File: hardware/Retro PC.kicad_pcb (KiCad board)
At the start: 2 copper layers, 160 x 160 mm, 70 parts, among them IC1 74HC00, IC10 W65C22, IC11 LCD-016N002L, IC2 W65C02, IC3 74HC138, IC4 SYSTEM ROM, IC5 AS6C62256A, IC6 W65C22, IC7 W65C51, IC8 TL7702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

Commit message: Working on layout
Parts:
- removed C19: 100nF, Capacitor_THT:C_Rect_L4.0mm_W2.5mm_P2.50mm
- removed J1: USB_B, TE_Connectivity:USB_B_TE_2923042_Horizontal
- added X2: USB_B, Connector_Custom:USB-B_TE_2923042_Horizontal, F.Cu at (220.2, 158.6)
- added X4: KEYBOARD, Connector_Custom:Mini-DIN_TE_Female_6Pin_2rows, F.Cu at (230.1, 178.0)
- X1: value ConBarrel -> DC IN; footprint Wuerth:BarrelJack_Wuerth_6941xx301002 -> Connector_Custom:BarrelJack_Wuerth_6941xx301002
- X3: renamed from J3; value Conn_02x20_Odd_Even -> Expansion
- moved C18 112.0 mm to (147.8, 187.6), turned to 90 degrees
- moved D9 67.1 mm to (204.4, 117.1), turned to 180 degrees
- moved R1 8.01 mm to (159.3, 81.3), turned to 90 degrees
- moved D8 7.24 mm to (163.7, 73.7), turned to 270 degrees
- moved D13 6.10 mm to (71.4, 73.5)
- moved R8 6.10 mm to (78.5, 69.3)
- moved X3 1.02 mm to (220.1, 72.6)
- moved IC5 0.07 mm to (109.9, 119.6)
- moved IC4 0.06 mm to (109.9, 87.8)
- moved C4 0.06 mm to (109.9, 108.9), turned to 0 degrees
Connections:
- net /IO/1MHz renamed /IO/Clock
- net /Processor/ModemReady renamed /Processor/~ModemReady
- D9 pad 1: /Processor/~IRQ -> /IO/~IRQ
- IC10 pad 10: Net-(IC10-Pad10) -> /LCD / PS2/LCD0
- IC10 pad 11: Net-(IC10-Pad11) -> /LCD / PS2/LCD1
- IC10 pad 12: Net-(IC10-Pad12) -> /LCD / PS2/LCD2
- IC10 pad 13: Net-(IC10-Pad13) -> (no net)
- IC10 pad 14: Net-(IC10-Pad14) -> (no net)
- IC10 pad 15: Net-(IC10-Pad15) -> (no net)
- IC10 pad 16: Net-(IC10-Pad16) -> /LCD / PS2/PS20
- IC10 pad 17: Net-(IC10-Pad17) -> /LCD / PS2/PS21
- IC10 pad 18: Net-(IC10-Pad18) -> (no net)
- IC10 pad 19: Net-(IC10-Pad19) -> (no net)
- IC10 pad 2: Net-(IC10-Pad2) -> /LCD / PS2/LCD3
- IC10 pad 3: Net-(IC10-Pad3) -> /LCD / PS2/LCD4
- IC10 pad 39: Net-(IC10-Pad39) -> (no net)
- IC10 pad 4: Net-(IC10-Pad4) -> /LCD / PS2/LCD5
- IC10 pad 40: Net-(IC10-Pad40) -> (no net)
- IC10 pad 5: Net-(IC10-Pad5) -> /LCD / PS2/LCD6
- IC10 pad 6: Net-(IC10-Pad6) -> /LCD / PS2/LCD7
- IC10 pad 7: Net-(IC10-Pad7) -> /LCD / PS2/LCD8
- IC10 pad 8: Net-(IC10-Pad8) -> /LCD / PS2/LCD9
- IC10 pad 9: Net-(IC10-Pad9) -> /LCD / PS2/LCD10
- IC11 pad 10: Net-(IC11-Pad10) -> /LCD / PS2/LCD6
- IC11 pad 11: Net-(IC11-Pad11) -> /LCD / PS2/LCD7
- IC11 pad 12: Net-(IC11-Pad12) -> /LCD / PS2/LCD8
- IC11 pad 13: Net-(IC11-Pad13) -> /LCD / PS2/LCD9
- IC11 pad 14: Net-(IC11-Pad14) -> /LCD / PS2/LCD10
- IC11 pad 4: Net-(IC11-Pad4) -> /LCD / PS2/LCD2
- IC11 pad 5: Net-(IC11-Pad5) -> /LCD / PS2/LCD1
- IC11 pad 6: Net-(IC11-Pad6) -> /LCD / PS2/LCD0
- IC11 pad 7: Net-(IC11-Pad7) -> /LCD / PS2/LCD3
- IC11 pad 8: Net-(IC11-Pad8) -> /LCD / PS2/LCD4
- IC11 pad 9: Net-(IC11-Pad9) -> /LCD / PS2/LCD5
- IC11 pad A1: Net-(IC11-PadA1) -> (no net)
- IC11 pad A2: Net-(IC11-PadA2) -> (no net)
- IC11 pad K1: Net-(IC11-PadK1) -> (no net)
- IC11 pad K2: Net-(IC11-PadK2) -> (no net)
- IC2 pad 1: /Processor/VPB -> (no net)
- IC2 pad 3: Net-(IC2-Pad3) -> (no net)
- IC2 pad 35: Net-(IC2-Pad35) -> (no net)
- IC2 pad 36: /Processor/BE -> (no net)
- IC2 pad 38: Net-(IC2-Pad38) -> (no net)
- IC2 pad 39: Net-(IC2-Pad39) -> (no net)
- IC2 pad 5: Net-(IC2-Pad5) -> (no net)
- IC2 pad 7: /Processor/SYNC -> (no net)
- IC3 pad 10: Net-(IC3-Pad10) -> (no net)
- IC3 pad 11: Net-(IC3-Pad11) -> (no net)
- IC3 pad 12: Net-(IC3-Pad12) -> (no net)
- IC3 pad 7: Net-(IC3-Pad7) -> (no net)
- IC3 pad 9: Net-(IC3-Pad9) -> (no net)
- IC6 pad 39: Net-(IC6-Pad39) -> (no net)
- IC6 pad 40: Net-(IC6-Pad40) -> (no net)
- IC7 pad 11: /Processor/ACIAReady -> (no net)
- IC7 pad 16: GND -> (no net)
- IC7 pad 5: Net-(IC7-Pad5) -> (no net)
- IC8 pad 6: Net-(IC8-Pad6) -> (no net)
- IC9 pad 10: Net-(IC9-Pad10) -> (no net)
- IC9 pad 12: Net-(IC9-Pad12) -> (no net)
- IC9 pad 13: Net-(IC9-Pad13) -> (no net)
- IC9 pad 14: Net-(IC9-Pad14) -> (no net)
- IC9 pad 26: Net-(IC9-Pad26) -> (no net)
- IC9 pad 27: Net-(IC9-Pad27) -> (no net)
- IC9 pad 28: Net-(IC9-Pad28) -> (no net)
- IC9 pad 6: Net-(IC9-Pad6) -> (no net)
- IC9 pad 9: Net-(IC9-Pad9) -> (no net)
- RV1 pad 3: Net-(RV1-Pad3) -> (no net)
- X3 pad 24: Net-(J3-Pad24) -> /IO/~IRQ
- X3 pad 26: Net-(J3-Pad26) -> (no net)
- X3 pad 28: Net-(J3-Pad28) -> (no net)
- X3 pad 30: Net-(J3-Pad30) -> (no net)
- X3 pad 32: Net-(J3-Pad32) -> (no net)
- X3 pad 33: Net-(J3-Pad33) -> (no net)
- X3 pad 34: Net-(J3-Pad34) -> (no net)
- X3 pad 35: Net-(J3-Pad35) -> (no net)
- X3 pad 36: Net-(J3-Pad36) -> (no net)
- X3 pad 37: Net-(J3-Pad37) -> (no net)
- X3 pad 38: Net-(J3-Pad38) -> (no net)
- XTAL1 pad 1: Net-(XTAL1-Pad1) -> (no net)
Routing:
- net /LCD / PS2/PS20: track 0.00 -> 98.2 mm, vias 0 -> 1
- net /LCD / PS2/PS21: track 0.00 -> 93.1 mm, vias 0 -> 1
- net /IO/D7: track 323.3 -> 402.6 mm, vias 12 -> 13
- net /IO/D6: track 327.3 -> 401.7 mm, vias 13 -> 14
- net /IO/D5: track 330.7 -> 398.2 mm, vias 13 -> 14
- net /IO/D4: track 334.5 -> 395.3 mm, vias 13 -> 14
- net /IO/D3: track 335.2 -> 391.5 mm, vias 13 -> 14
- net /IO/R~W: track 180.3 -> 232.3 mm, vias 9 -> 11
- net /IO/D2: track 352.7 -> 401.7 mm, vias 11 -> 12
- net /IO/Clock: track 153.2 -> 202.1 mm, vias 5 -> 8
- net /IO/D1: track 361.5 -> 404.8 mm, vias 11 -> 12
- net /Processor/~IRQ_ACIA: track 37.4 -> 76.8 mm
- net /IO/~RESET: track 365.0 -> 404.3 mm, vias 8 -> 10
- net /IO/D0: track 370.0 -> 404.0 mm, vias 11 -> 12
- net /IO/~IRQ: track 0.00 -> 33.6 mm, vias 0 -> 1
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
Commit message: First version of the layout
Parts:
- U1: value R-785.0-0.5 -> R-785.0-1.0
- X2: value USB_B -> SERIAL
- moved D14 4.42 mm to (146.4, 169.0), turned to 180 degrees
- moved XTAL2 0.66 mm to (189.2, 146.2)
- moved R4 0.53 mm to (195.5, 141.0)
- moved C8 0.51 mm to (183.8, 146.2)
- moved C11 0.38 mm to (117.1, 55.2)
- moved C17 0.33 mm to (130.8, 55.2)
- moved R9 0.18 mm to (123.2, 52.0)
- moved R5 0.14 mm to (109.5, 52.0)
- moved SW1 0.12 mm to (110.6, 44.0)
- moved SW4 0.06 mm to (124.3, 44.0)
- turned C18 to 270 degrees
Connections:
- IC10 pad 13: (no net) -> Net-(IC10-Pad13)
- IC10 pad 14: (no net) -> Net-(IC10-Pad14)
- IC10 pad 15: (no net) -> Net-(IC10-Pad15)
- IC10 pad 18: (no net) -> Net-(IC10-Pad18)
- IC10 pad 19: (no net) -> Net-(IC10-Pad19)
- IC10 pad 39: (no net) -> Net-(IC10-Pad39)
- IC10 pad 40: (no net) -> Net-(IC10-Pad40)
- IC11 pad A1: (no net) -> Net-(IC11-PadA1)
- IC11 pad A2: (no net) -> Net-(IC11-PadA2)
- IC11 pad K1: (no net) -> Net-(IC11-PadK1)
- IC11 pad K2: (no net) -> Net-(IC11-PadK2)
- IC2 pad 1: (no net) -> /Processor/VPB
- IC2 pad 3: (no net) -> Net-(IC2-Pad3)
- IC2 pad 35: (no net) -> Net-(IC2-Pad35)
- IC2 pad 36: (no net) -> /Processor/BE
- IC2 pad 38: (no net) -> Net-(IC2-Pad38)
- IC2 pad 39: (no net) -> Net-(IC2-Pad39)
- IC2 pad 5: (no net) -> Net-(IC2-Pad5)
- IC2 pad 7: (no net) -> /Processor/SYNC
- IC3 pad 10: (no net) -> Net-(IC3-Pad10)
- IC3 pad 11: (no net) -> Net-(IC3-Pad11)
- IC3 pad 12: (no net) -> Net-(IC3-Pad12)
- IC3 pad 7: (no net) -> Net-(IC3-Pad7)
- IC3 pad 9: (no net) -> Net-(IC3-Pad9)
- IC6 pad 39: (no net) -> Net-(IC6-Pad39)
- IC6 pad 40: (no net) -> Net-(IC6-Pad40)
- IC7 pad 11: (no net) -> /Processor/~ReceiverReady
- IC7 pad 16: (no net) -> /Processor/~Carrier
- IC7 pad 5: (no net) -> Net-(IC7-Pad5)
- IC8 pad 6: (no net) -> Net-(IC8-Pad6)
- IC9 pad 10: (no net) -> Net-(IC9-Pad10)
- IC9 pad 12: (no net) -> Net-(IC9-Pad12)
- IC9 pad 13: (no net) -> Net-(IC9-Pad13)
- IC9 pad 14: (no net) -> Net-(IC9-Pad14)
- IC9 pad 26: (no net) -> Net-(IC9-Pad26)
- IC9 pad 27: (no net) -> Net-(IC9-Pad27)
- IC9 pad 28: (no net) -> Net-(IC9-Pad28)
- IC9 pad 6: (no net) -> Net-(IC9-Pad6)
- IC9 pad 9: (no net) -> Net-(IC9-Pad9)
- RV1 pad 3: (no net) -> Net-(RV1-Pad3)
- X2 pad 1: (no net) -> Net-(X2-Pad1)
- X3 pad 26: (no net) -> Net-(X3-Pad26)
- X3 pad 28: (no net) -> Net-(X3-Pad28)
- X3 pad 30: (no net) -> Net-(X3-Pad30)
- X3 pad 32: (no net) -> Net-(X3-Pad32)
- X3 pad 33: (no net) -> Net-(X3-Pad33)
- X3 pad 34: (no net) -> Net-(X3-Pad34)
- X3 pad 35: (no net) -> Net-(X3-Pad35)
- X3 pad 36: (no net) -> Net-(X3-Pad36)
- X3 pad 37: (no net) -> Net-(X3-Pad37)
- X3 pad 38: (no net) -> Net-(X3-Pad38)
- X4 pad 3: (no net) -> Net-(X4-Pad3)
- X4 pad 6: (no net) -> Net-(X4-Pad6)
- X4 pad 7: (no net) -> GND
- XTAL1 pad 1: (no net) -> Net-(XTAL1-Pad1)
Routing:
- net /LCD / PS2/LCD10: track 0.00 -> 93.8 mm, vias 0 -> 1
- net /LCD / PS2/LCD9: track 0.00 -> 93.4 mm, vias 0 -> 1
- net /LCD / PS2/LCD8: track 0.00 -> 92.9 mm, vias 0 -> 1
- net /LCD / PS2/LCD7: track 0.00 -> 92.5 mm, vias 0 -> 1
- net /LCD / PS2/LCD6: track 0.00 -> 92.0 mm, vias 0 -> 1
- net /LCD / PS2/LCD5: track 0.00 -> 91.6 mm, vias 0 -> 1
- net /LCD / PS2/LCD4: track 0.00 -> 91.4 mm, vias 0 -> 1
- net /LCD / PS2/LCD3: track 0.00 -> 90.9 mm, vias 0 -> 1
- net /Processor/~IRQ_ACIA: track 76.8 -> 166.9 mm, vias 2 -> 6
- net /LCD / PS2/LCD0: track 0.00 -> 83.1 mm, vias 0 -> 3
- net Net-(IC11-Pad3): track 0.00 -> 81.9 mm, vias 0 -> 2
- net /LCD / PS2/LCD1: track 0.00 -> 79.2 mm, vias 0 -> 3
- net /LCD / PS2/LCD2: track 0.00 -> 75.6 mm, vias 0 -> 3
- net /Processor/~CS_VIA_2: track 76.8 -> 75.7 mm
- net Net-(C8-Pad1): track 17.4 -> 18.5 mm
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
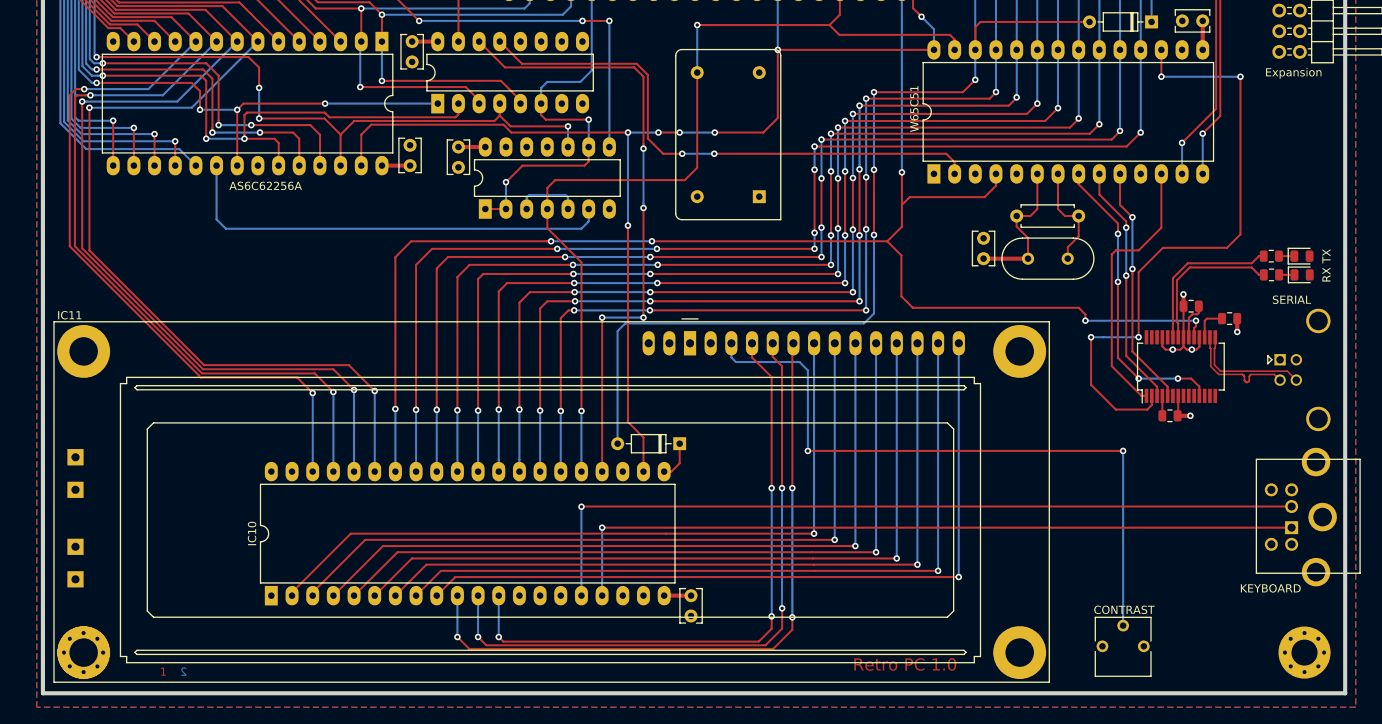
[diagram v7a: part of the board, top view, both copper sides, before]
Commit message: Replace LCD
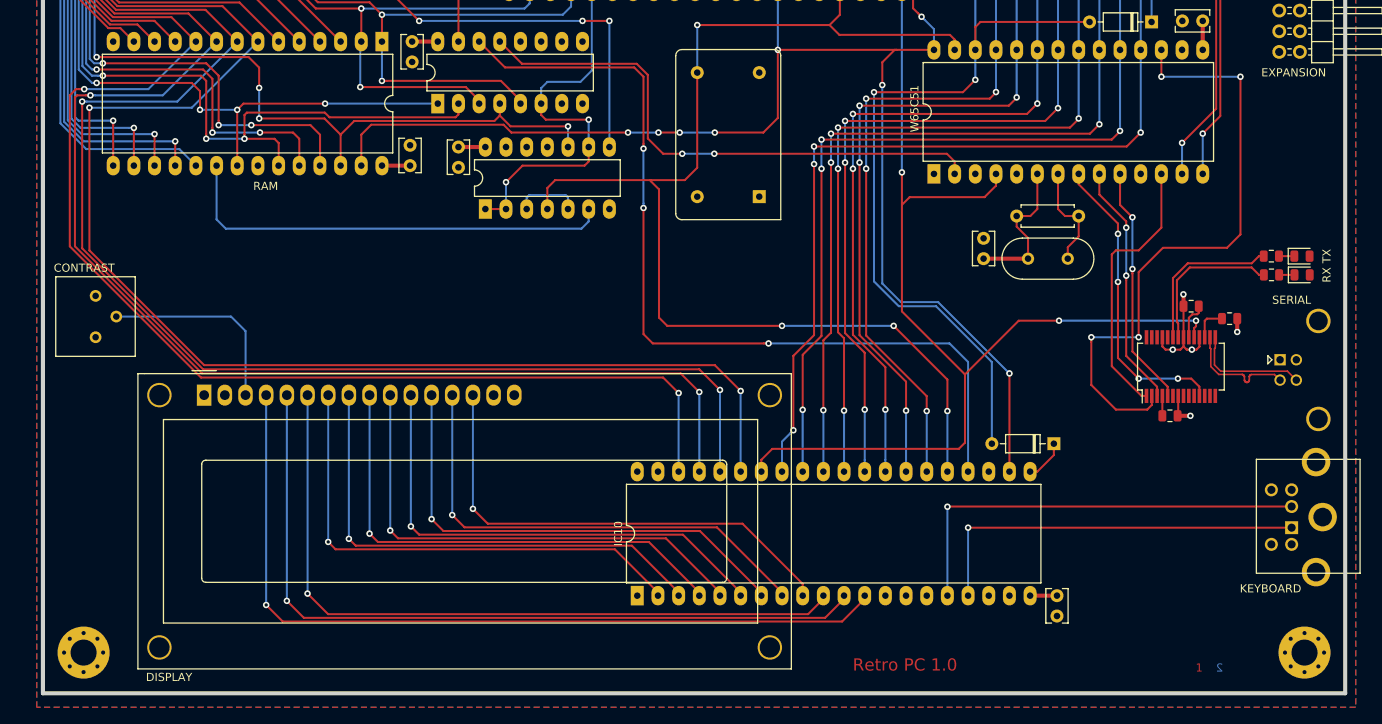
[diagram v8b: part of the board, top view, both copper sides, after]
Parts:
- removed IC11: LCD-016N002L, Display:LCD-016N002L
- added DS1: DISPLAY, Display:WC1602A, F.Cu at (88.0, 163.0)
- IC5: value AS6C62256A -> RAM
- RV1: footprint Potentiometer_THT:Potentiometer_Vishay_T73YP_Vertical -> Potentiometer:Bourns_3386T_Vertical
- X3: value Expansion -> EXPANSION
- moved RV1 134.3 mm to (74.7, 155.9), turned to 0 degrees
- moved D14 46.0 mm to (192.4, 169.0)
- moved C18 45.0 mm to (192.8, 187.6)
- moved IC10 45.0 mm to (141.2, 187.6)
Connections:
- IC10 pad 13: Net-(IC10-Pad13) -> (no net)
- IC10 pad 14: Net-(IC10-Pad14) -> (no net)
- IC10 pad 15: Net-(IC10-Pad15) -> (no net)
- IC10 pad 18: Net-(IC10-Pad18) -> (no net)
- IC10 pad 19: Net-(IC10-Pad19) -> (no net)
- IC10 pad 39: Net-(IC10-Pad39) -> (no net)
- IC10 pad 40: Net-(IC10-Pad40) -> (no net)
- IC2 pad 1: /Processor/VPB -> (no net)
- IC2 pad 3: Net-(IC2-Pad3) -> (no net)
- IC2 pad 35: Net-(IC2-Pad35) -> (no net)
- IC2 pad 36: /Processor/BE -> (no net)
- IC2 pad 38: Net-(IC2-Pad38) -> (no net)
- IC2 pad 39: Net-(IC2-Pad39) -> (no net)
- IC2 pad 5: Net-(IC2-Pad5) -> (no net)
- IC2 pad 7: /Processor/SYNC -> (no net)
- IC3 pad 10: Net-(IC3-Pad10) -> (no net)
- IC3 pad 11: Net-(IC3-Pad11) -> (no net)
- IC3 pad 12: Net-(IC3-Pad12) -> (no net)
- IC3 pad 7: Net-(IC3-Pad7) -> (no net)
- IC3 pad 9: Net-(IC3-Pad9) -> (no net)
- IC6 pad 39: Net-(IC6-Pad39) -> (no net)
- IC6 pad 40: Net-(IC6-Pad40) -> (no net)
- IC7 pad 11: /Processor/~ReceiverReady -> (no net)
- IC7 pad 16: /Processor/~Carrier -> (no net)
- IC7 pad 5: Net-(IC7-Pad5) -> (no net)
- IC8 pad 6: Net-(IC8-Pad6) -> (no net)
- IC9 pad 10: Net-(IC9-Pad10) -> (no net)
- IC9 pad 12: Net-(IC9-Pad12) -> (no net)
- IC9 pad 13: Net-(IC9-Pad13) -> (no net)
- IC9 pad 14: Net-(IC9-Pad14) -> (no net)
- IC9 pad 26: Net-(IC9-Pad26) -> (no net)
- IC9 pad 27: Net-(IC9-Pad27) -> (no net)
- IC9 pad 28: Net-(IC9-Pad28) -> (no net)
- IC9 pad 6: Net-(IC9-Pad6) -> (no net)
- IC9 pad 9: Net-(IC9-Pad9) -> (no net)
- RV1 pad 3: Net-(RV1-Pad3) -> (no net)
- X2 pad 1: Net-(X2-Pad1) -> (no net)
- X3 pad 26: Net-(X3-Pad26) -> (no net)
- X3 pad 28: Net-(X3-Pad28) -> (no net)
- X3 pad 30: Net-(X3-Pad30) -> (no net)
- X3 pad 32: Net-(X3-Pad32) -> (no net)
- X3 pad 33: Net-(X3-Pad33) -> (no net)
- X3 pad 34: Net-(X3-Pad34) -> (no net)
- X3 pad 35: Net-(X3-Pad35) -> (no net)
- X3 pad 36: Net-(X3-Pad36) -> (no net)
- X3 pad 37: Net-(X3-Pad37) -> (no net)
- X3 pad 38: Net-(X3-Pad38) -> (no net)
- X4 pad 3: Net-(X4-Pad3) -> (no net)
- X4 pad 6: Net-(X4-Pad6) -> (no net)
- XTAL1 pad 1: Net-(XTAL1-Pad1) -> (no net)
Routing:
- net Net-(DS1-Pad3): track 81.9 -> 24.5 mm, vias 2 -> 0
- net /IO/~RESET: track 403.5 -> 356.0 mm, vias 10 -> 7
- net /IO/D0: track 404.0 -> 357.9 mm, vias 12 -> 8
- net /IO/D1: track 404.8 -> 359.4 mm, vias 12 -> 8
- net /LCD / PS2/PS21: track 93.1 -> 48.1 mm
- net /IO/A3: track 322.1 -> 367.1 mm
- net /IO/A2: track 319.8 -> 364.8 mm
- net /IO/A1: track 374.9 -> 419.9 mm
- net /IO/A0: track 372.3 -> 417.3 mm
- net /LCD / PS2/PS20: track 98.2 -> 53.3 mm
- net /IO/D2: track 401.7 -> 357.1 mm, vias 12 -> 8
- net /IO/D3: track 391.5 -> 348.0 mm, vias 14 -> 10
- net /IO/D4: track 395.3 -> 354.4 mm, vias 14 -> 10
- net /IO/D5: track 398.2 -> 359.6 mm, vias 14 -> 10
- net /IO/D6: track 401.6 -> 365.3 mm, vias 14 -> 10
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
